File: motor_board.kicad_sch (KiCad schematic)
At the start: 31 parts, among them J1 MyRIO_C, J10 ESCON_24-2, J11 Conn_01x02, J12 Conn_01x05, J13 Conn_01x03, J2 BNC, J3 BNC, J4 BNC, J5 Conn_01x04, J6 Barrel_Jack_Switch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

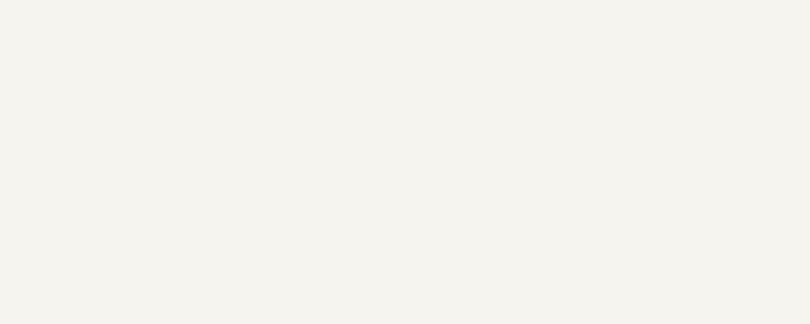
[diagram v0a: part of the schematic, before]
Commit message: added a couple mounting holes and updated the motor mount
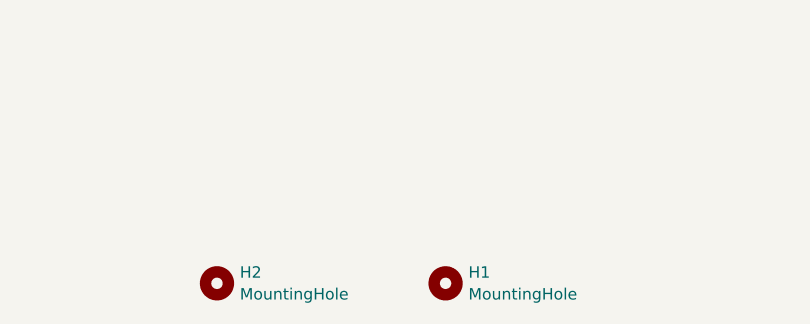
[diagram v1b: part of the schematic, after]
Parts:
- added H1, H2: MountingHole, motor_board:MountingHole_#6, symbol Mechanical:MountingHole

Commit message: changed to a bidirectional TVS diode for protection on the amp analog inputs
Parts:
- D1, D3: value D_TVS -> P6KE16CA; DigiKey P/N 13-P6KE62A/B-ND -> 13-P6KE16CA/B-ND
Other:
- moved on the sheet: D1, D3, J12

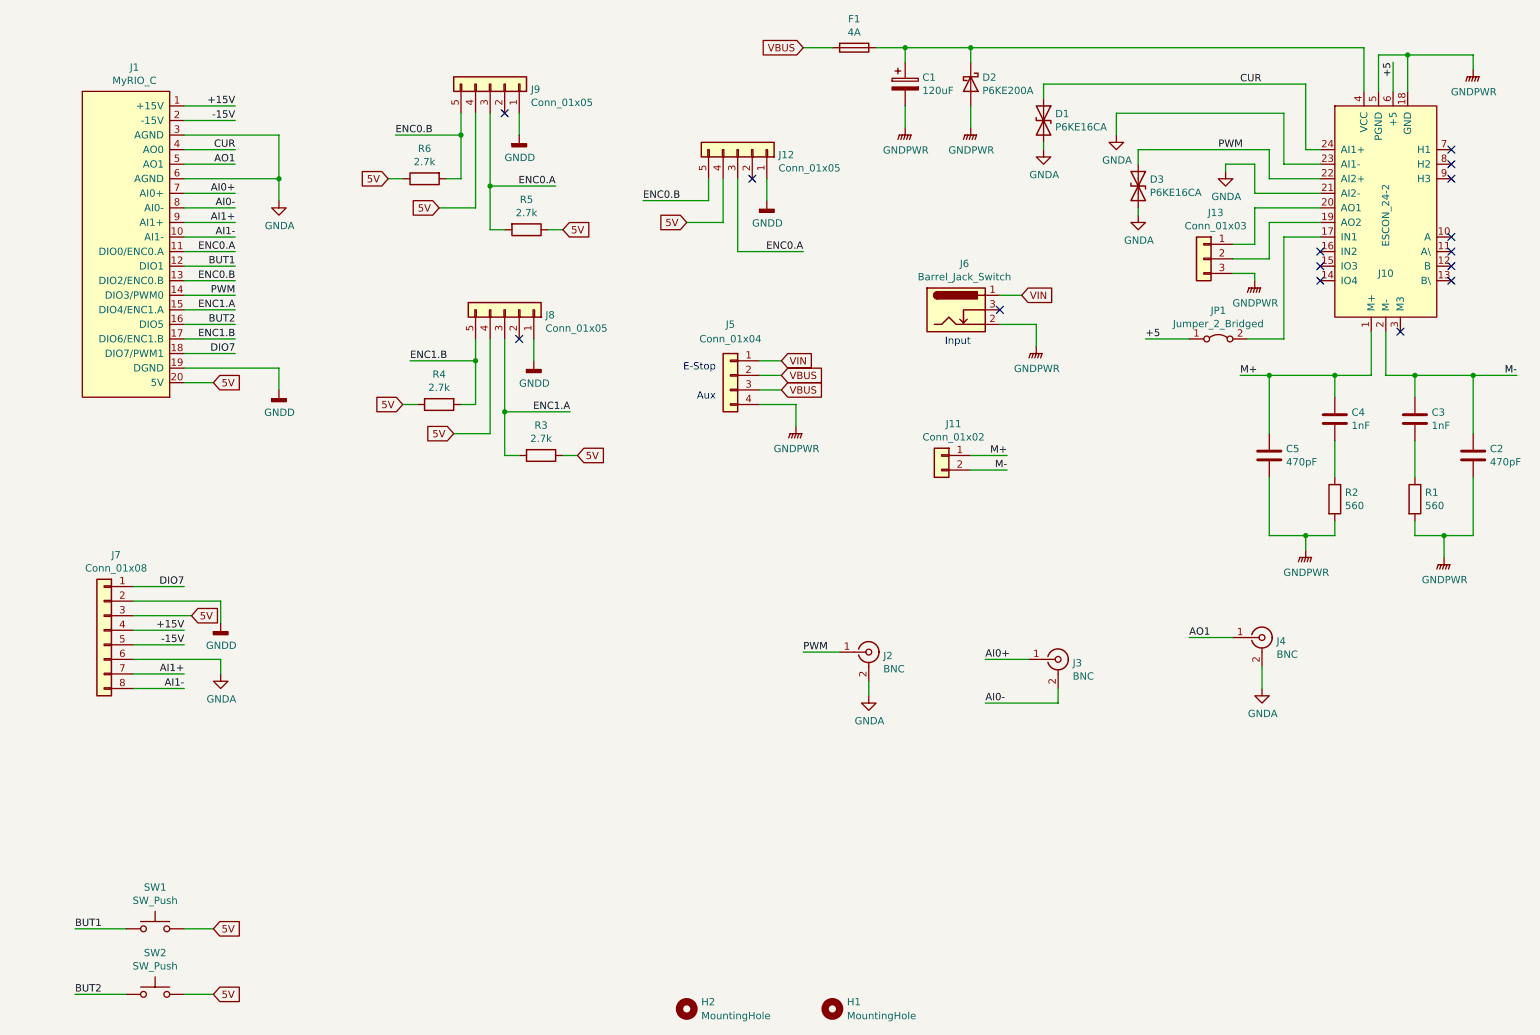
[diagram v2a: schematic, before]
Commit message: updated the board with a 90 degree twisted motor and 5 bncs plus amp input switch and trim.
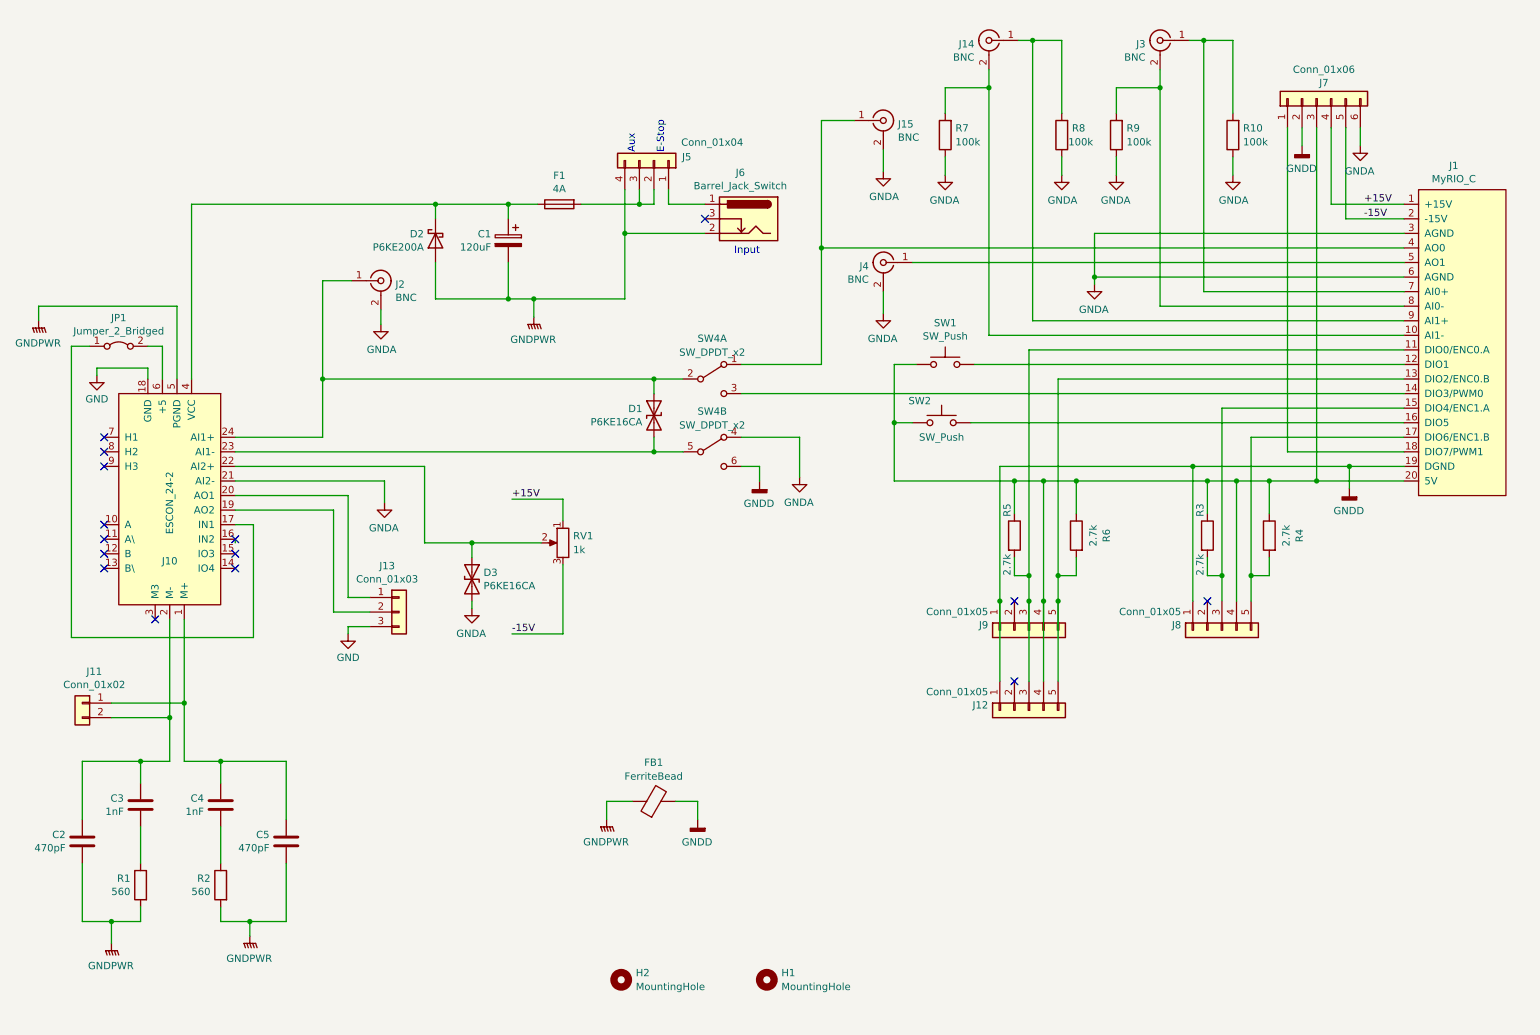
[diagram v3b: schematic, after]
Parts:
- added FB1: FerriteBead, Inductor_THT:L_Axial_L7.0mm_D3.3mm_P10.16mm_Horizontal_Fastron_MICC, symbol Device:FerriteBead
- added J14, J15: BNC, motor_board:Vertical_BNC_Amphenol_112536, symbol Connector:Conn_Coaxial
- added R10, R7, R8, R9: 100k, Resistor_THT:R_Axial_DIN0204_L3.6mm_D1.6mm_P5.08mm_Horizontal, symbol Device:R
- added RV1: 1k, motor_board:CUI PTN06-E Pot, symbol Device:R_Potentiometer
- added SW4: SW_DPDT_x2, motor_board:TE Connectivity MHS DPDT Slide Switch, symbol Switch:SW_DPDT_x2
- J7: value Conn_01x08 -> Conn_01x06; footprint Connector_PinSocket_2.54mm:PinSocket_1x08_P2.54mm_Vertical -> Connector_PinSocket_2.54mm:PinSocket_1x06_P2.54mm_Vertical; symbol Connector_Generic:Conn_01x08 -> Connector_Generic:Conn_01x06; DigiKey P/N S7006-ND -> S7004-ND
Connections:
- net +15V: now also RV1.1
- net -15V: now also RV1.3
- net GNDA: now also J15.2 (Ext), R10.1, R7.1, R8.1, R9.1, SW4.4 (A); no longer D1.2 (A2), J10.23 (AI1-)
- net GNDD: now also FB1.2, SW4.6 (C)
- net GNDPWR: now also FB1.1; no longer J10.18 (GND), J13.3 (Pin_3)
- net at J10.17 (IN1): now also JP1.1 (A); no longer JP1.2 (B)
- net +5: no longer names the net of J10.6 (+5)
- net +5: now also JP1.2 (B); no longer JP1.1 (A)
- net 5V: no longer names the net of J1.20 (5V), J12.4 (Pin_4), J7.3 (Pin_3), J8.4 (Pin_4), J9.4 (Pin_4), R3.1, R4.1, R5.1, R6.1, SW1.2, SW2.2
- net AI0+: no longer names the net of J1.7 (AI0+), J3.1 (In)
- net AI0+: now also R10.2
- net AI0-: no longer names the net of J1.8 (AI0-), J3.2 (Ext)
- net AI0-: now also R9.2
- net AI1+: no longer names the net of J1.9 (AI1+)
- net AI1+: now also J14.1 (In), R8.2; no longer J7.7 (Pin_7)
- net AI1-: no longer names the net of J1.10 (AI1-)
- net AI1-: now also J14.2 (Ext), R7.2; no longer J7.8 (Pin_8)
- net AO1: no longer names the net of J1.5 (AO1), J4.1 (In)
- net BUT1: no longer names the net of J1.12 (DIO1), SW1.1
- net BUT2: no longer names the net of J1.16 (DIO5), SW2.1
- net CUR: no longer names the net of D1.1 (A1), J10.24 (AI1+)
- net CUR: now also J2.1 (In), SW4.2 (B); no longer J1.4 (AO0)
- net DIO7: no longer names the net of J1.18 (DIO7/PWM1), J7.1 (Pin_1)
- net ENC0.A: no longer names the net of J1.11 (DIO0/ENC0.A), J12.3 (Pin_3), J9.3 (Pin_3), R5.2
- net ENC0.B: no longer names the net of J1.13 (DIO2/ENC0.B), J12.5 (Pin_5), J9.5 (Pin_5), R6.2
- net ENC1.A: no longer names the net of J1.15 (DIO4/ENC1.A), J8.3 (Pin_3), R3.2
- net ENC1.B: no longer names the net of J1.17 (DIO6/ENC1.B), J8.5 (Pin_5), R4.2
- net M+: no longer names the net of C4.1, C5.1, J10.1 (M+), J11.1 (Pin_1)
- net M-: no longer names the net of C2.1, C3.1, J10.2 (M-), J11.2 (Pin_2)
- net PWM: no longer names the net of D3.1 (A1), J10.22 (AI2+)
- net PWM: now also RV1.2; no longer J1.14 (DIO3/PWM0), J2.1 (In)
- net VBUS: no longer names the net of F1.2, J5.2 (Pin_2), J5.3 (Pin_3)
- net VIN: no longer names the net of J5.1 (Pin_1), J6.1
- new net: D1.2 (A2), J10.23 (AI1-), SW4.5 (B)
- new net: J1.14 (DIO3/PWM0), SW4.3 (C)
- new net: J1.4 (AO0), J15.1 (In), SW4.1 (A)
- new net GND: J10.18 (GND), J13.3 (Pin_3)
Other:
- moved on the sheet: C1, C2, C3, C4, C5, D1, D2, D3, F1, H1, H2, J1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

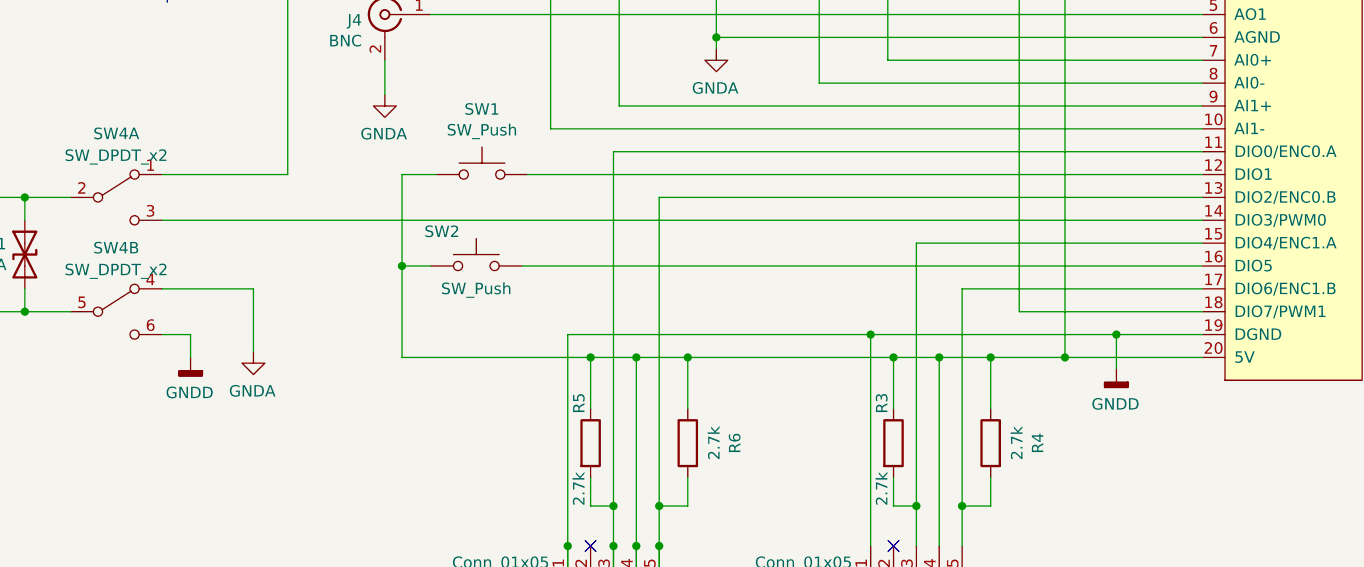
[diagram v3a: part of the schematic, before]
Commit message: added a resistor divider to the PWM amp input
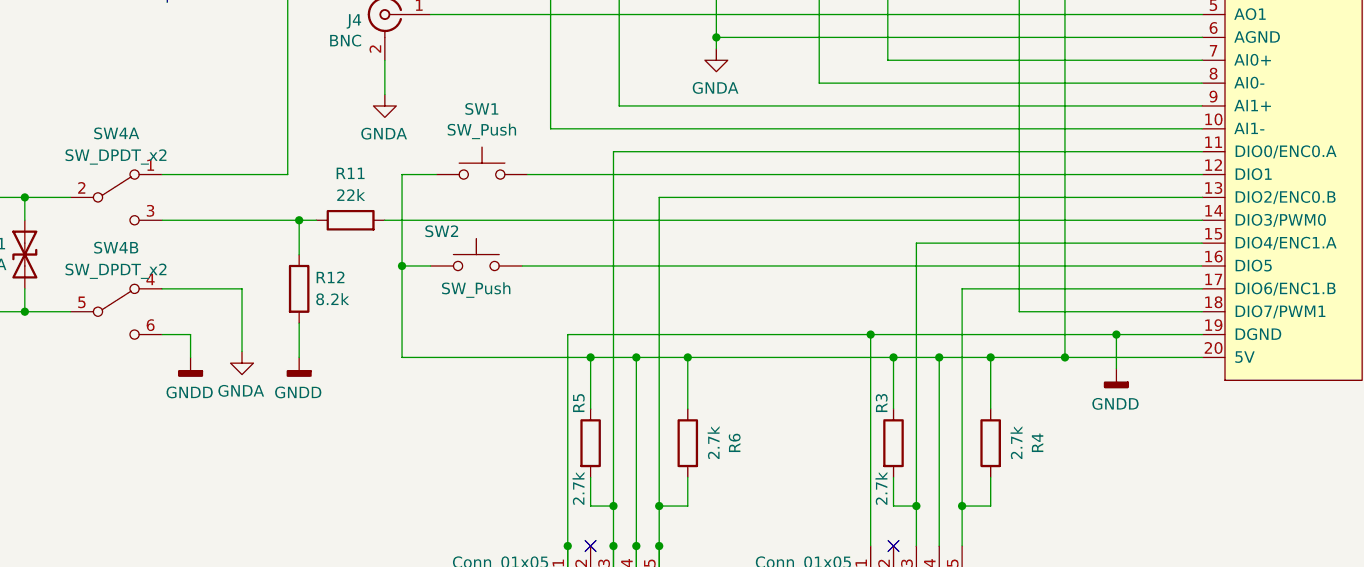
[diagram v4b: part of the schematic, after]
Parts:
- added R11: 22k, Resistor_THT:R_Axial_DIN0204_L3.6mm_D1.6mm_P5.08mm_Horizontal, symbol Device:R
- added R12: 8.2k, Resistor_THT:R_Axial_DIN0204_L3.6mm_D1.6mm_P5.08mm_Horizontal, symbol Device:R
- C1: footprint Capacitor_THT:CP_Radial_D8.0mm_P3.50mm -> Resistor_THT:R_Axial_DIN0204_L3.6mm_D1.6mm_P5.08mm_Horizontal
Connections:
- net GNDD: now also R12.2
- net at J1.14 (DIO3/PWM0): now also R11.2; no longer SW4.3 (C)
- new net: R11.1, R12.1, SW4.3 (C)
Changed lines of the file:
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@@
   (junction (at 187.96 95.885) (diameter 0) (color 0 0 0 0)
+  )
+  (junction (at 155.575 80.645) (diameter 0) (color 0 0 0 0)
   )
   (junction (at 40.64 137.16) (diameter 0) (color 0 0 0 0)
@@
     (stroke (width 0) (type default))
   )
+  (wire (pts (xy 155.575 92.075) (xy 155.575 95.885))
+    (stroke (width 0) (type default))
+  )
   (wire (pts (xy 165.1 38.1) (xy 165.1 41.91))
     (stroke (width 0) (type default))
@@
     (stroke (width 0) (type default))
   )
-  (wire (pts (xy 255.905 80.645) (xy 140.335 80.645))
+  (wire (pts (xy 255.905 80.645) (xy 165.1 80.645))
     (stroke (width 0) (type default))
   )
@@
     (stroke (width 0) (type default))
   )
+  (wire (pts (xy 155.575 80.645) (xy 155.575 84.455))
+    (stroke (width 0) (type default))
+  )
   (wire (pts (xy 104.14 64.135) (xy 120.015 64.135))
     (stroke (width 0) (type default))
@@
     (stroke (width 0) (type default))
   )
-  (wire (pts (xy 150.495 88.265) (xy 150.495 95.25))
+  (wire (pts (xy 149.225 88.265) (xy 149.225 95.25))
     (stroke (width 0) (type default))
   )
@@
     (stroke (width 0) (type default))
   )
+  (wire (pts (xy 157.48 80.645) (xy 155.575 80.645))
+    (stroke (width 0) (type default))
+  )
   (wire (pts (xy 255.905 67.945) (xy 191.135 67.945))
     (stroke (width 0) (type default))
@@
     (stroke (width 0) (type default))
   )
-  (wire (pts (xy 140.335 88.265) (xy 150.495 88.265))
+  (wire (pts (xy 140.335 88.265) (xy 149.225 88.265))
     (stroke (width 0) (type default))
   )
@@
   )
   (wire (pts (xy 60.96 162.56) (xy 60.96 172.72))
+    (stroke (width 0) (type default))
+  )
+  (wire (pts (xy 155.575 80.645) (xy 140.335 80.645))
     (stroke (width 0) (type default))
   )
@@
       (effects (font (size 1.27 1.27)) (justify left))
     )
-    (property "Footprint" "Capacitor_THT:CP_Radial_D8.0mm_P3.50mm" (at 98.7298 57.785 0)
+    (property "Footprint" "Resistor_THT:R_Axial_DIN0204_L3.6mm_D1.6mm_P5.08mm_Horizontal" (at 98.7298 57.785 0)
       (effects (font (size 1.27 1.27)) hide)
     )
@@
     )
   )
-  (symbol (lib_id "power:GNDA") (at 150.495 95.25 0) (mirror y) (unit 1)
-    (in_bom yes) (on_board yes) (dnp no)
-    (property "Reference" "#PWR0114" (at 150.495 101.6 0)
-      (effects (font (size 1.27 1.27)) hide)
-    )
-    (property "Value" "GNDA" (at 150.368 99.6442 0)
-      (effects (font (size 1.27 1.27)))
-    )
-    (property "Footprint" "" (at 150.495 95.25 0)
-      (effects (font (size 1.27 1.27)) hide)
-    )
-    (property "Datasheet" "" (at 150.495 95.25 0)
+  (symbol (lib_id "power:GNDA") (at 149.225 95.25 0) (mirror y) (unit 1)
+    (in_bom yes) (on_board yes) (dnp no)
+    (property "Reference" "#PWR0114" (at 149.225 101.6 0)
+      (effects (font (size 1.27 1.27)) hide)
+    )
+    (property "Value" "GNDA" (at 149.098 99.6442 0)
+      (effects (font (size 1.27 1.27)))
+    )
+    (property "Footprint" "" (at 149.225 95.25 0)
+      (effects (font (size 1.27 1.27)) hide)
+    )
+    (property "Datasheet" "" (at 149.225 95.25 0)
       (effects (font (size 1.27 1.27)) hide)
     )
@@
     )
   )
+  (symbol (lib_id "Device:R") (at 155.575 88.265 0) (unit 1)
+    (in_bom yes) (on_board yes) (dnp no) (fields_autoplaced)
+    (property "Reference" "R12" (at 157.353 87.0529 0)
+      (effects (font (size 1.27 1.27)) (justify left))
+    )
+    (property "Value" "8.2k" (at 157.353 89.4771 0)
+      (effects (font (size 1.27 1.27)) (justify left))
+    )
+    (property "Footprint" "Resistor_THT:R_Axial_DIN0204_L3.6mm_D1.6mm_P5.08mm_Horizontal" (at 153.797 88.265 90)
+      (effects (font (size 1.27 1.27)) hide)
+    )
+    (property "Datasheet" "~" (at 155.575 88.265 0)
+      (effects (font (size 1.27 1.27)) hide)
+    )
+    (property "DigiKey P/N" "13-MFR-12FTF52-8K2CT-ND" (at 155.575 88.265 0)
+      (effects (font (size 1.27 1.27)) hide)
+    )
+    (pin "2")
+    (pin "1")
+    (instances
+      (project "motor_board"
+        (path "/6c00be26-d4b1-4ad6-ac8d-0612cd96db96"
+          (reference "R12") (unit 1)
+        )
+      )
+    )
+  )
   (symbol (lib_id "power:GNDA") (at 165.1 41.91 0) (unit 1)
     (in_bom yes) (on_board yes) (dnp no)
@@
     )
   )
+  (symbol (lib_id "Device:R") (at 161.29 80.645 90) (unit 1)
+    (in_bom yes) (on_board yes) (dnp no) (fields_autoplaced)
+    (property "Reference" "R11" (at 161.29 75.4847 90)
+      (effects (font (size 1.27 1.27)))
+    )
+    (property "Value" "22k" (at 161.29 77.9089 90)
+      (effects (font (size 1.27 1.27)))
+    )
+    (property "Footprint" "Resistor_THT:R_Axial_DIN0204_L3.6mm_D1.6mm_P5.08mm_Horizontal" (at 161.29 82.423 90)
+      (effects (font (size 1.27 1.27)) hide)
+    )
+    (property "Datasheet" "~" (at 161.29 80.645 0)
+      (effects (font (size 1.27 1.27)) hide)
+    )
+    (property "DigiKey P/N" "13-MFR-12FTF52-22KCT-ND" (at 161.29 80.645 0)
+      (effects (font (size 1.27 1.27)) hide)
+    )
+    (pin "1")
+    (pin "2")
+    (instances
+      (project "motor_board"
+        (path "/6c00be26-d4b1-4ad6-ac8d-0612cd96db96"
+          (reference "R11") (unit 1)
+        )
+      )
+    )
+  )
   (symbol (lib_id "power:GNDA") (at 196.215 42.545 0) (unit 1)
     (in_bom yes) (on_board yes) (dnp no)
@@
         )
       )
+    )
+  )
+  (symbol (lib_id "power:GNDD") (at 155.575 95.885 0) (mirror y) (unit 1)
+    (in_bom yes) (on_board yes) (dnp no)
+    (property "Reference" "#PWR013" (at 155.575 102.235 0)
+      (effects (font (size 1.27 1.27)) hide)
+    )
+    (property "Value" "GNDD" (at 155.4734 99.822 0)
+      (effects (font (size 1.27 1.27)))
+    )
+    (property "Footprint" "" (at 155.575 95.885 0)
+      (effects (font (size 1.27 1.27)) hide)
+    )
+    (property "Datasheet" "" (at 155.575 95.885 0)
+      (effects (font (size 1.27 1.27)) hide)
+    )
+    (pin "1")
+    (instances
+      (project "motor_board"
+        (path "/6c00be26-d4b1-4ad6-ac8d-0612cd96db96"
+          (reference "#PWR013") (unit 1)
+        )
+      )
